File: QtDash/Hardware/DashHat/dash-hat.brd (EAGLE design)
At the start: 120.9 x 66.8 mm, 166 parts, among them IC1 LMV614, IC2 MCP3X083008, IC3 MCP23017SS, IC4 LM358D, IC5 IL300, IC6 TSV912D, IC7 IL300, IC8 TSV912D, IC9 DS1374, J1 CONN_20X2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

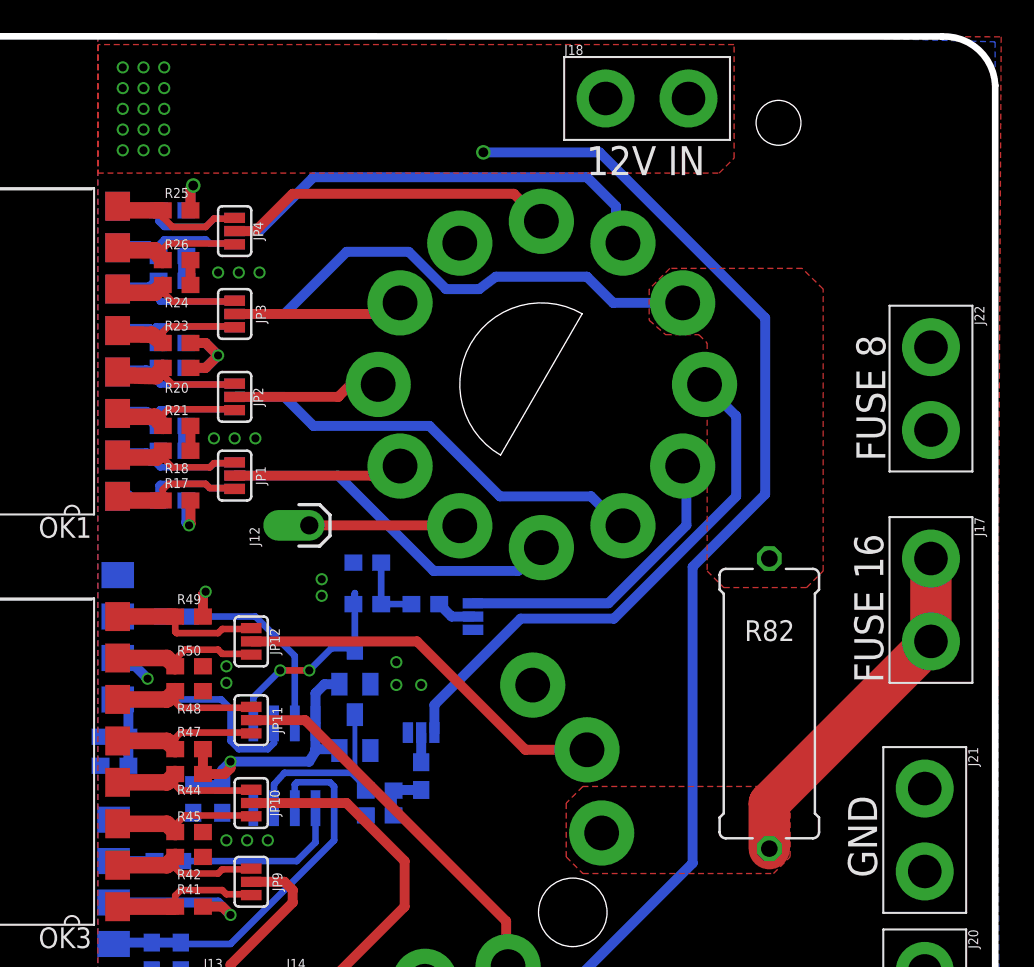
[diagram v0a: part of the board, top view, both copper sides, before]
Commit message: bugfix/hardware-revA-issues: 	- moved D+ resistor back to switched 12V supply 	- added second switched 12V header 	- D+ resistor moved and 12Vin plane extended
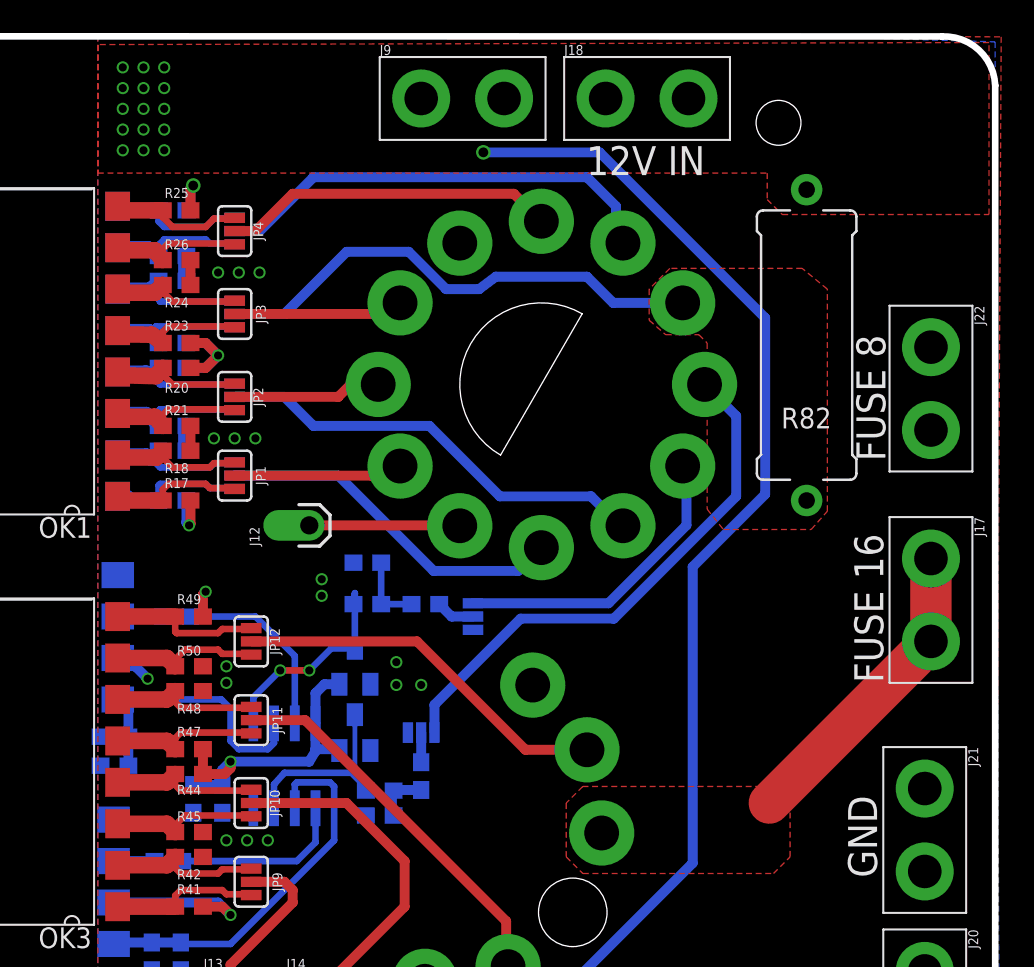
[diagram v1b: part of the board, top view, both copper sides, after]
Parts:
- added J9: (no value), SparkFun-Connectors:1X02_XTRA_BIG
- R82: value (none) -> RES_D+; device resistor:0617/17 -> digital_dash:0617/17
- moved R82 22.1 mm to (109.5, 47.9), turned to 90 degrees
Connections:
- net 12V: now also J9.1, J9.2, R82.2
- net 12V-FUSE_16: no longer R82.2
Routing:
- net 12V-FUSE_16: track 21.9 -> 19.1 mm
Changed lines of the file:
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@@
 <element name="R78" library="digital_dash" package="0603" value="1k" x="9.652" y="59.69" rot="R180"/>
 <element name="R79" library="digital_dash" package="0603" value="1k" x="14.732" y="59.69" rot="R180"/>
-<element name="R82" library="resistor" package="0617/17" value="" x="107.188" y="25.908" smashed="yes" rot="R270">
-<attribute name="NAME" x="105.664" y="29.7434" size="1.27" layer="25" ratio="10"/>
-<attribute name="VALUE" x="106.4768" y="32.004" size="1.27" layer="27" ratio="10" rot="R270"/>
+<element name="R82" library="digital_dash" package="0617/17" value="RES_D+" x="109.474" y="47.879" smashed="yes" rot="R90">
+<attribute name="NAME" x="110.998" y="44.0436" size="1.27" layer="25" ratio="10" rot="R180"/>
+<attribute name="VALUE" x="110.1852" y="41.783" size="1.27" layer="27" ratio="10" rot="R90"/>
 </element>
 <element name="J19" library="SparkFun-Connectors" package="1X02_XTRA_BIG" value="" x="9.652" y="22.733" rot="R270"/>
@@
 <element name="J17" library="SparkFun-Connectors" package="1X02_XTRA_BIG" value="" x="117.094" y="32.258" rot="R270"/>
 <element name="J18" library="SparkFun-Connectors" package="1X02_XTRA_BIG" value="" x="99.695" y="62.992"/>
+<element name="J9" library="SparkFun-Connectors" package="1X02_XTRA_BIG" value="" x="88.392" y="62.992"/>
 </elements>
 <signals>
@@
 <vertex x="66.04" y="66.294"/>
 <vertex x="66.04" y="58.42"/>
-<vertex x="104.113190625" y="58.42"/>
-<vertex x="105.029" y="59.335809375"/>
-<vertex x="105.029" y="66.294"/>
+<vertex x="107.061" y="58.42"/>
+<vertex x="107.061" y="56.795809375"/>
+<vertex x="107.976809375" y="55.88"/>
+<vertex x="120.65" y="55.88"/>
+<vertex x="120.65" y="66.421"/>
 </polygon>
 <via x="68.834" y="64.897" extent="1-16" drill="0.5"/>
@@
 <contactref element="J18" pad="2"/>
 <contactref element="J18" pad="1"/>
+<contactref element="R82" pad="2"/>
+<contactref element="J9" pad="2"/>
+<contactref element="J9" pad="1"/>
 </signal>
 <signal name="OUT1">
@@
 <polygon width="0.4064" layer="1" isolate="0.3048" orphans="yes" thermals="no">
 <vertex x="103.378" y="48.006"/>
-<vertex x="103.378" y="34.036"/>
-<vertex x="104.394" y="33.02"/>
-<vertex x="109.474" y="33.02"/>
-<vertex x="110.49" y="34.036"/>
-<vertex x="110.49" y="51.308"/>
+<vertex x="103.378" y="37.8219"/>
+<vertex x="104.3699" y="36.576"/>
+<vertex x="109.7521" y="36.576"/>
+<vertex x="110.744" y="37.6949"/>
+<vertex x="110.744" y="51.308"/>
 <vertex x="109.20181875" y="52.578"/>
 <vertex x="101.092" y="52.578"/>
@@
 <signal name="12V-FUSE_16">
 <contactref element="J7" pad="A"/>
-<contactref element="R82" pad="2"/>
 <polygon width="0.3048" layer="1" isolate="0.3048" thermals="no">
 <vertex x="108.458" y="20.828"/>
@@
 <wire x1="117.094" y1="29.718" x2="117.094" y2="34.798" width="2.54" layer="1"/>
 <wire x1="117.094" y1="29.718" x2="107.188" y2="19.812" width="2.54" layer="1"/>
-<wire x1="107.188" y1="19.812" x2="107.188" y2="17.018" width="2.54" layer="1"/>
 </signal>
 <signal name="OD_LAMP_AUTO_P">

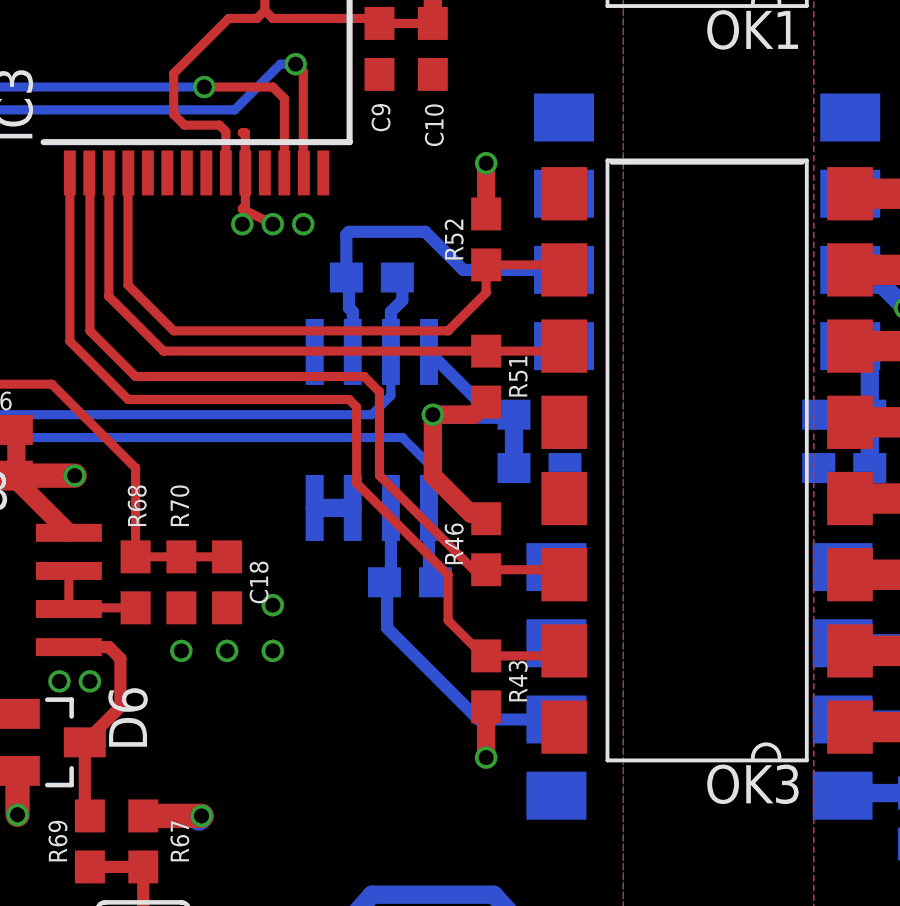
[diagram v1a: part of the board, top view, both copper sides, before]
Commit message: bugfix/hardware-revA-issues: 	- output of IL300s were oscillating under load -- added 100n capacitor (bodged on revA) 	- 12V inputs are only 0-3.3V signals -- K3 used to compensate for different for now
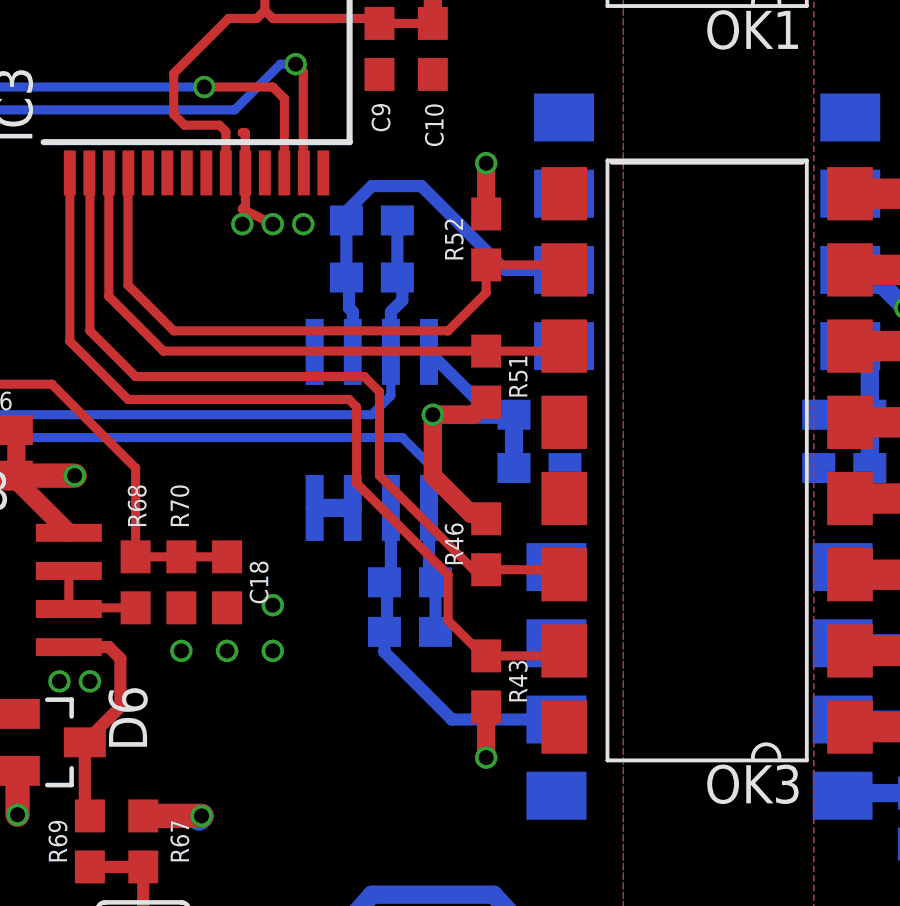
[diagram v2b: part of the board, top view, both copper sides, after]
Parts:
- added C21, C22: 100n, digital_dash:0603
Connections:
- removed net N$18: IC5.6, IC6.2, R56.1
- new net N$10: C21.2, IC5.6, IC6.2, R56.1
- net N$27: now also C22.1
- net SIG_3V3_IN1: now also C21.1
- net SIG_3V3_IN2: now also C22.2
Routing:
- net N$10: track 0.00 -> 11.8 mm
- net N$18: track 11.2 -> 0.00 mm
- net SIG_3V3_IN2: track 26.0 -> 27.9 mm
- net N$27: track 11.8 -> 13.5 mm
- net SIG_3V3_IN1: track 29.2 -> 30.9 mm
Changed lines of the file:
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@@
 <grid distance="5" unitdist="mil" unit="mil" style="lines" multiple="1" display="yes" altdistance="1" altunitdist="mil" altunit="mil"/>
 <layers>
-<layer number="1" name="Top" color="4" fill="1" visible="yes" active="yes"/>
-<layer number="2" name="Route2" color="1" fill="3" visible="yes" active="yes"/>
+<layer number="1" name="Top" color="4" fill="1" visible="no" active="yes"/>
+<layer number="2" name="Route2" color="1" fill="3" visible="no" active="yes"/>
 <layer number="3" name="Route3" color="4" fill="3" visible="no" active="no"/>
 <layer number="4" name="Route4" color="1" fill="4" visible="no" active="no"/>
@@
 <layer number="13" name="Route13" color="4" fill="5" visible="no" active="no"/>
 <layer number="14" name="Route14" color="1" fill="6" visible="no" active="no"/>
-<layer number="15" name="Route15" color="4" fill="6" visible="yes" active="yes"/>
+<layer number="15" name="Route15" color="4" fill="6" visible="no" active="yes"/>
 <layer number="16" name="Bottom" color="9" fill="1" visible="yes" active="yes"/>
 <layer number="17" name="Pads" color="2" fill="1" visible="yes" active="yes"/>
@@
 <element name="J18" library="SparkFun-Connectors" package="1X02_XTRA_BIG" value="" x="99.695" y="62.992"/>
 <element name="J9" library="SparkFun-Connectors" package="1X02_XTRA_BIG" value="" x="88.392" y="62.992"/>
+<element name="C21" library="digital_dash" package="0603" value="100n" x="52.578" y="16.637" rot="MR0"/>
+<element name="C22" library="digital_dash" package="0603" value="100n" x="51.308" y="30.353" rot="MR180"/>
 </elements>
 <signals>
@@
 <wire x1="52.324" y1="23.114" x2="53.213" y2="22.225" width="0.3048" layer="16"/>
 <wire x1="53.213" y1="22.225" x2="53.213" y2="20.768" width="0.3048" layer="16"/>
-</signal>
-<signal name="N$18">
-<contactref element="IC5" pad="6"/>
-<contactref element="R56" pad="1"/>
-<contactref element="IC6" pad="2"/>
-<wire x1="51.728" y1="18.288" x2="51.943" y2="18.249" width="0.4064" layer="16"/>
-<wire x1="51.943" y1="18.249" x2="51.943" y2="20.768" width="0.4064" layer="16"/>
-<wire x1="51.943" y1="18.249" x2="51.816" y2="18.122" width="0.4064" layer="16"/>
-<wire x1="51.816" y1="18.122" x2="51.816" y2="16.764" width="0.4064" layer="16"/>
-<wire x1="51.816" y1="16.764" x2="54.864" y2="13.716" width="0.4064" layer="16"/>
-<wire x1="54.864" y1="13.716" x2="57.46" y2="13.716" width="0.4064" layer="16"/>
+<contactref element="C21" pad="1"/>
+<wire x1="53.428" y1="16.637" x2="53.428" y2="18.288" width="0.4064" layer="16"/>
 </signal>
 <signal name="N$6">
@@
 <wire x1="51.308" y1="23.876" x2="51.943" y2="24.511" width="0.3048" layer="16"/>
 <wire x1="51.943" y1="24.511" x2="51.943" y2="25.968" width="0.3048" layer="16"/>
+<contactref element="C22" pad="2"/>
+<wire x1="52.158" y1="28.448" x2="52.158" y2="30.353" width="0.4064" layer="16"/>
 </signal>
 <signal name="N$27">
@@
 <wire x1="50.546" y1="27.432" x2="50.546" y2="28.36" width="0.4064" layer="16"/>
 <wire x1="50.546" y1="28.36" x2="50.458" y2="28.448" width="0.4064" layer="16"/>
-<wire x1="54.356" y1="28.702" x2="53.086" y2="29.972" width="0.4064" layer="16"/>
-<wire x1="53.086" y1="29.972" x2="50.546" y2="29.972" width="0.4064" layer="16"/>
-<wire x1="50.546" y1="29.972" x2="50.458" y2="29.884" width="0.4064" layer="16"/>
-<wire x1="50.458" y1="29.884" x2="50.458" y2="28.448" width="0.4064" layer="16"/>
-<wire x1="54.356" y1="28.702" x2="57.714" y2="28.702" width="0.4064" layer="16"/>
+<contactref element="C22" pad="1"/>
+<wire x1="50.458" y1="28.448" x2="50.458" y2="30.353" width="0.4064" layer="16"/>
+<wire x1="57.714" y1="28.702" x2="55.753" y2="28.702" width="0.4064" layer="16"/>
+<wire x1="55.753" y1="28.702" x2="52.959" y2="31.496" width="0.4064" layer="16"/>
+<wire x1="52.959" y1="31.496" x2="51.308" y2="31.496" width="0.4064" layer="16"/>
+<wire x1="51.308" y1="31.496" x2="50.458" y2="30.646" width="0.4064" layer="16"/>
+<wire x1="50.458" y1="30.646" x2="50.458" y2="30.353" width="0.4064" layer="16"/>
 </signal>
 <signal name="GND-ISO">
@@
 </polygon>
 </signal>
+<signal name="N$10">
+<contactref element="C21" pad="2"/>
+<contactref element="IC5" pad="6"/>
+<contactref element="R56" pad="1"/>
+<contactref element="IC6" pad="2"/>
+<wire x1="51.728" y1="18.288" x2="51.943" y2="18.249" width="0.4064" layer="16"/>
+<wire x1="51.943" y1="18.249" x2="51.943" y2="20.768" width="0.4064" layer="16"/>
+<wire x1="51.943" y1="18.249" x2="51.816" y2="18.122" width="0.4064" layer="16"/>
+<wire x1="51.816" y1="18.122" x2="51.816" y2="16.725" width="0.4064" layer="16"/>
+<wire x1="53.975" y1="13.716" x2="57.46" y2="13.716" width="0.4064" layer="16"/>
+<wire x1="53.975" y1="13.716" x2="51.728" y2="15.963" width="0.4064" layer="16"/>
+<wire x1="51.728" y1="15.963" x2="51.728" y2="16.637" width="0.4064" layer="16"/>
+<wire x1="51.728" y1="16.637" x2="51.816" y2="16.725" width="0.4064" layer="16"/>
+</signal>
 </signals>
